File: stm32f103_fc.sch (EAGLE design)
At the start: 39 parts, among them IC1 STM32F10XCXT6, U1 RT9193-33GB, Y1 8MHz, Y2 32.768MHz

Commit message: added more lable
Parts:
- removed C5, C6, C7, C8: 1nF, SparkFun-Capacitors:1.0NF/1000PF-0603-50V-10%
- added C22: 100nF, SparkFun-Capacitors:1.0NF/1000PF-0603-50V-10%
- added SWD: (no value), SparkFun-Connectors:CONN_04
- C1: value 1nF -> 100nF
- C12: value 0.1uF -> 1000nF
- C2: value 1nF -> 10uF
- R3, R4: value 1k -> 70ohm
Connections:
- new net N$28: IC1POWER.VSS_2
- new net N$30: IC1POWER.VDD_2
- new net N$31: IC1POWER.VDD_1
- new net PA0: IC1PORTA_L.PA0
- new net PA1: IC1PORTA_L.PA1
- new net PA10: IC1PORTA_H.PA10
- new net PA15: IC1PORTA_H.PA15
- new net PA2: IC1PORTA_L.PA2
- new net PA3: IC1PORTA_L.PA3
- new net PA4: IC1PORTA_L.PA4
- new net PA5: IC1PORTA_L.PA5
- new net PA6: IC1PORTA_L.PA6
- new net PA7: IC1PORTA_L.PA7
- new net PA8: IC1PORTA_H.PA8
- new net PA9: IC1PORTA_H.PA9
- new net PB0: IC1PORTB_L.PB0
- new net PB1: IC1PORTB_L.PB1
- new net PB10: IC1PORTB_H.PB10
- new net PB11: IC1PORTB_H.PB11
- new net PB12: IC1PORTB_H.PB12
- new net PB13: IC1PORTB_H.PB13
- new net PB14: IC1PORTB_H.PB14
- new net PB15: IC1PORTB_H.PB15
- new net PB3: IC1PORTB_L.PB3
- new net PB4: IC1PORTB_L.PB4
- new net PB5: IC1PORTB_L.PB5
- new net PB6: IC1PORTB_L.PB6
- new net PB7: IC1PORTB_L.PB7
- new net PB8: IC1PORTB_H.PB8
- new net PB9: IC1PORTB_H.PB9
- new net SWDCLK: IC1PORTA_H.PA14, SWD.2
- new net SWDIO: IC1PORTA_H.PA13, SWD.3
- new net VBAT: IC1AN_POWER.VBAT
- net GND: now also C22.2, IC1AN_POWER.VSSA, IC1POWER.VSS_1, IC1POWER.VSS_3, SWD.1
- net PC14: now also IC1PORTC.PC14
- net PC15: now also IC1PORTC.PC15
- net VCC3V3: now also C22.1, IC1AN_POWER.VDDA, SWD.4
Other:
- moved on the sheet: C9, J1

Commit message: added more lable
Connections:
- net 5V: now also J2.3
- net GND: now also J1.1, J1.2, J2.2
- net PA0: now also J1.16
- net PA1: now also J1.15
- net PA10: now also J2.14
- net PA11: now also J2.13
- net PA12: now also J2.12
- net PA15: now also J2.11
- net PA2: now also J1.14
- net PA3: now also J1.13
- net PA4: now also J1.12
- net PA5: now also J1.11
- net PA6: now also J1.10
- net PA7: now also J1.9
- net PA8: now also J2.16
- net PA9: now also J2.15
- net PB0: now also J1.8
- net PB1: now also J1.7
- net PB10: now also J1.6
- net PB11: now also J1.5
- net PB12: now also J2.20
- net PB13: now also J2.19
- net PB14: now also J2.18
- net PB15: now also J2.17
- net PB3: now also J2.10
- net PB4: now also J2.9
- net PB5: now also J2.8
- net PB6: now also J2.7
- net PB7: now also J2.6
- net PB8: now also J2.5
- net PB9: now also J2.4
- net PC13: now also J1.19
- net PC14: now also J1.18
- net PC15: now also J1.17
- net RESET: now also J1.4
- net VBAT: now also J1.20
- net VCC3V3: now also J1.3, J2.1
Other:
- moved on the sheet: J1, J2

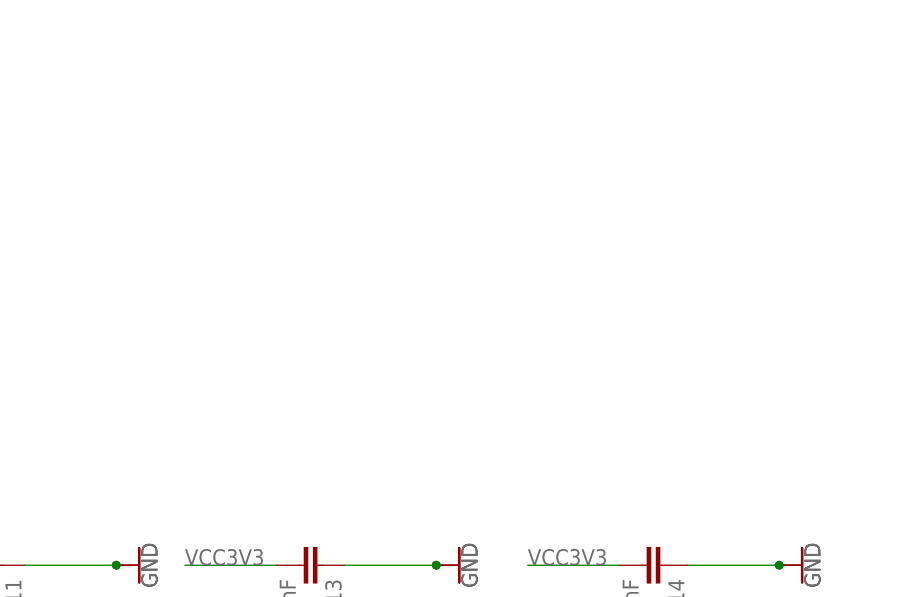
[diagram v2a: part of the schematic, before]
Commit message: added mpu-9250
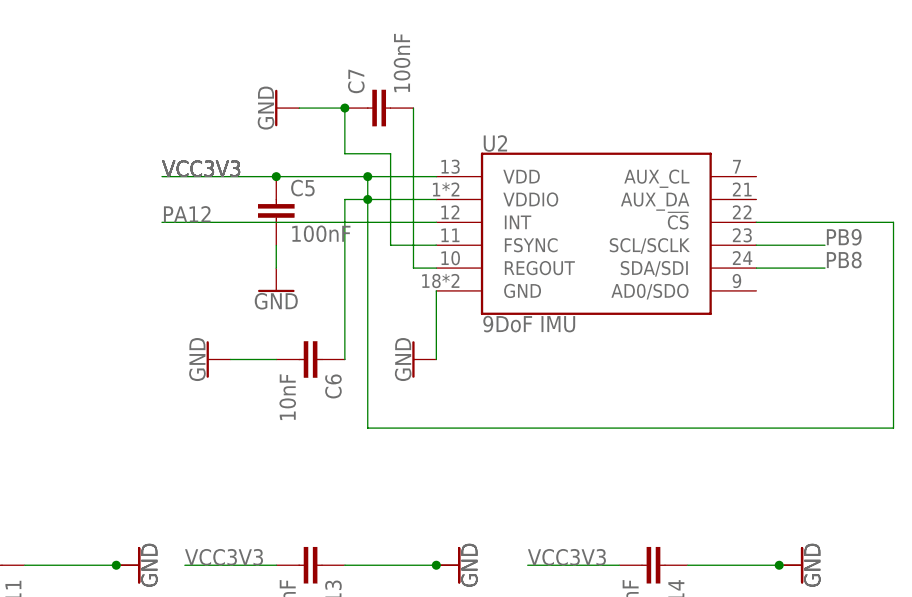
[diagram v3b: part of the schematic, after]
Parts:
- added C5, C7: 100nF, SparkFun-Capacitors:1.0UF-0805-25V-(+80/-20%)
- added C6: 10nF, SparkFun-Capacitors:1.0UF-0805-25V-(+80/-20%)
- added U2: 9DoF IMU, SparkFun-Sensors:MPU-9250
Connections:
- new net N$11: C7.2, U2.REGOUT
- net GND: now also C5.2, C6.2, C7.1, U2.FSYNC, U2.GND
- net PA12: now also U2.INT
- net PB8: now also U2.SDA/SDI
- net PB9: now also U2.SCL/SCLK
- net VCC3V3: now also C5.1, C6.1, U2.!CS, U2.VDD, U2.VDDIO
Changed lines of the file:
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@@
 <part name="GND23" library="SparkFun-PowerSymbols" library_urn="urn:adsk.eagle:library:530" deviceset="GND" device=""/>
 <part name="GND24" library="SparkFun-PowerSymbols" library_urn="urn:adsk.eagle:library:530" deviceset="GND" device=""/>
+<part name="U2" library="SparkFun-Sensors" deviceset="MPU-9250" device="" value="9DoF IMU"/>
+<part name="C5" library="SparkFun-Capacitors" library_urn="urn:adsk.eagle:library:510" deviceset="1.0UF" device="-0805-25V-(+80/-20%)" package3d_urn="urn:adsk.eagle:package:37429/1" value="100nF"/>
+<part name="GND25" library="SparkFun-PowerSymbols" library_urn="urn:adsk.eagle:library:530" deviceset="GND" device=""/>
+<part name="GND26" library="SparkFun-PowerSymbols" library_urn="urn:adsk.eagle:library:530" deviceset="GND" device=""/>
+<part name="C6" library="SparkFun-Capacitors" library_urn="urn:adsk.eagle:library:510" deviceset="1.0UF" device="-0805-25V-(+80/-20%)" package3d_urn="urn:adsk.eagle:package:37429/1" value="10nF"/>
+<part name="GND27" library="SparkFun-PowerSymbols" library_urn="urn:adsk.eagle:library:530" deviceset="GND" device=""/>
+<part name="C7" library="SparkFun-Capacitors" library_urn="urn:adsk.eagle:library:510" deviceset="1.0UF" device="-0805-25V-(+80/-20%)" package3d_urn="urn:adsk.eagle:package:37429/1" value="100nF"/>
+<part name="GND28" library="SparkFun-PowerSymbols" library_urn="urn:adsk.eagle:library:530" deviceset="GND" device=""/>
 </parts>
 <sheets>
@@
 <instance part="GND24" gate="1" x="22.86" y="7.62" smashed="yes" rot="R270">
 <attribute name="VALUE" x="22.606" y="7.62" size="1.778" layer="96" rot="R270" align="top-center"/>
+</instance>
+<instance part="U2" gate="G$1" x="175.26" y="127" smashed="yes">
+<attribute name="NAME" x="162.56" y="137.414" size="1.778" layer="95" font="vector"/>
+<attribute name="VALUE" x="162.56" y="119.126" size="1.778" layer="96" font="vector" align="top-left"/>
+</instance>
+<instance part="C5" gate="G$1" x="139.7" y="129.54" smashed="yes">
+<attribute name="NAME" x="141.224" y="132.461" size="1.778" layer="95" font="vector"/>
+<attribute name="VALUE" x="141.224" y="127.381" size="1.778" layer="96" font="vector"/>
+</instance>
+<instance part="GND25" gate="1" x="139.7" y="121.92" smashed="yes">
+<attribute name="VALUE" x="139.7" y="121.666" size="1.778" layer="96" align="top-center"/>
+</instance>
+<instance part="GND26" gate="1" x="154.94" y="114.3" smashed="yes" rot="R270">
+<attribute name="VALUE" x="154.686" y="114.3" size="1.778" layer="96" rot="R270" align="top-center"/>
+</instance>
+<instance part="C6" gate="G$1" x="142.24" y="114.3" smashed="yes" rot="R270">
+<attribute name="NAME" x="145.161" y="112.776" size="1.778" layer="95" font="vector" rot="R270"/>
+<attribute name="VALUE" x="140.081" y="112.776" size="1.778" layer="96" font="vector" rot="R270"/>
+</instance>
+<instance part="GND27" gate="1" x="132.08" y="114.3" smashed="yes" rot="R270">
+<attribute name="VALUE" x="131.826" y="114.3" size="1.778" layer="96" rot="R270" align="top-center"/>
+</instance>
+<instance part="C7" gate="G$1" x="152.4" y="142.24" smashed="yes" rot="R90">
+<attribute name="NAME" x="149.479" y="143.764" size="1.778" layer="95" font="vector" rot="R90"/>
+<attribute name="VALUE" x="154.559" y="143.764" size="1.778" layer="96" font="vector" rot="R90"/>
+</instance>
+<instance part="GND28" gate="1" x="139.7" y="142.24" smashed="yes" rot="R270">
+<attribute name="VALUE" x="139.446" y="142.24" size="1.778" layer="96" rot="R270" align="top-center"/>
 </instance>
 </instances>
@@
 <wire x1="-63.5" y1="58.42" x2="-71.12" y2="58.42" width="0.1524" layer="91"/>
 <label x="-71.12" y="58.42" size="1.778" layer="95"/>
+</segment>
+<segment>
+<pinref part="U2" gate="G$1" pin="VDD"/>
+<wire x1="157.48" y1="134.62" x2="149.86" y2="134.62" width="0.1524" layer="91"/>
+<label x="127" y="134.62" size="1.778" layer="95"/>
+<label x="127" y="134.62" size="1.778" layer="95"/>
+<label x="127" y="134.62" size="1.778" layer="95"/>
+<label x="127" y="134.62" size="1.778" layer="95"/>
+<pinref part="C5" gate="G$1" pin="1"/>
+<wire x1="149.86" y1="134.62" x2="139.7" y2="134.62" width="0.1524" layer="91"/>
+<wire x1="139.7" y1="134.62" x2="127" y2="134.62" width="0.1524" layer="91"/>
+<junction x="139.7" y="134.62"/>
+<pinref part="U2" gate="G$1" pin="!CS"/>
+<wire x1="193.04" y1="129.54" x2="208.28" y2="129.54" width="0.1524" layer="91"/>
+<wire x1="208.28" y1="129.54" x2="208.28" y2="106.68" width="0.1524" layer="91"/>
+<wire x1="208.28" y1="106.68" x2="149.86" y2="106.68" width="0.1524" layer="91"/>
+<wire x1="149.86" y1="106.68" x2="149.86" y2="132.08" width="0.1524" layer="91"/>
+<pinref part="U2" gate="G$1" pin="VDDIO"/>
+<wire x1="149.86" y1="132.08" x2="157.48" y2="132.08" width="0.1524" layer="91"/>
+<wire x1="149.86" y1="132.08" x2="147.32" y2="132.08" width="0.1524" layer="91"/>
+<junction x="149.86" y="132.08"/>
+<wire x1="149.86" y1="132.08" x2="149.86" y2="134.62" width="0.1524" layer="91"/>
+<junction x="149.86" y="134.62"/>
+<wire x1="147.32" y1="132.08" x2="147.32" y2="114.3" width="0.1524" layer="91"/>
+<pinref part="C6" gate="G$1" pin="1"/>
 </segment>
 </net>
@@
 <pinref part="J2" gate="G$1" pin="2"/>
 </segment>
+<segment>
+<pinref part="C5" gate="G$1" pin="2"/>
+<pinref part="GND25" gate="1" pin="GND"/>
+<wire x1="139.7" y1="127" x2="139.7" y2="124.46" width="0.1524" layer="91"/>
+</segment>
+<segment>
+<pinref part="U2" gate="G$1" pin="GND"/>
+<wire x1="157.48" y1="121.92" x2="157.48" y2="114.3" width="0.1524" layer="91"/>
+<pinref part="GND26" gate="1" pin="GND"/>
+</segment>
+<segment>
+<pinref part="C6" gate="G$1" pin="2"/>
+<pinref part="GND27" gate="1" pin="GND"/>
+<wire x1="139.7" y1="114.3" x2="134.62" y2="114.3" width="0.1524" layer="91"/>
+</segment>
+<segment>
+<pinref part="C7" gate="G$1" pin="1"/>
+<pinref part="GND28" gate="1" pin="GND"/>
+<wire x1="142.24" y1="142.24" x2="147.32" y2="142.24" width="0.1524" layer="91"/>
+<pinref part="U2" gate="G$1" pin="FSYNC"/>
+<wire x1="157.48" y1="127" x2="152.4" y2="127" width="0.1524" layer="91"/>
+<wire x1="152.4" y1="127" x2="152.4" y2="137.16" width="0.1524" layer="91"/>
+<wire x1="152.4" y1="137.16" x2="147.32" y2="137.16" width="0.1524" layer="91"/>
+<wire x1="147.32" y1="137.16" x2="147.32" y2="142.24" width="0.1524" layer="91"/>
+<junction x="147.32" y="142.24"/>
+</segment>
 </net>
 <net name="5V" class="0">
@@
 <pinref part="J2" gate="G$1" pin="12"/>
 </segment>
+<segment>
+<pinref part="U2" gate="G$1" pin="INT"/>
+<wire x1="157.48" y1="129.54" x2="127" y2="129.54" width="0.1524" layer="91"/>
+<label x="127" y="129.54" size="1.778" layer="95"/>
+</segment>
 </net>
 <net name="N$7" class="0">
@@
 <pinref part="J2" gate="G$1" pin="5"/>
 </segment>
+<segment>
+<pinref part="U2" gate="G$1" pin="SDA/SDI"/>
+<wire x1="193.04" y1="124.46" x2="200.66" y2="124.46" width="0.1524" layer="91"/>
+<label x="200.66" y="124.46" size="1.778" layer="95"/>
+</segment>
 </net>
 <net name="PB9" class="0">
@@
 <pinref part="J2" gate="G$1" pin="4"/>
 </segment>
+<segment>
+<pinref part="U2" gate="G$1" pin="SCL/SCLK"/>
+<wire x1="193.04" y1="127" x2="200.66" y2="127" width="0.1524" layer="91"/>
+<label x="200.66" y="127" size="1.778" layer="95"/>
+</segment>
 </net>
 <net name="PB10" class="0">
@@
 </segment>
 </net>
+<net name="N$11" class="0">
+<segment>
+<pinref part="U2" gate="G$1" pin="REGOUT"/>
+<wire x1="157.48" y1="124.46" x2="154.94" y2="124.46" width="0.1524" layer="91"/>
+<pinref part="C7" gate="G$1" pin="2"/>
+<wire x1="154.94" y1="124.46" x2="154.94" y2="142.24" width="0.1524" layer="91"/>
+</segment>
+</net>

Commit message: done some auto routing
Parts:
- added J4: (no value), SparkFun-Connectors:CONN_023.5MM
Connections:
- net 5V: now also J4.2
- net GND: now also J4.1
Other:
- note added: "to IMU clk"
- note added: "to IMU data"
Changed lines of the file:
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@@
 <part name="GND6" library="SparkFun-PowerSymbols" library_urn="urn:adsk.eagle:library:530" deviceset="GND" device=""/>
 <part name="GND7" library="SparkFun-PowerSymbols" library_urn="urn:adsk.eagle:library:530" deviceset="GND" device=""/>
-<part name="SUPPLY1" library="SparkFun-PowerSymbols" library_urn="urn:adsk.eagle:library:530" deviceset="5V" device=""/>
 <part name="C3" library="SparkFun-Capacitors" library_urn="urn:adsk.eagle:library:510" deviceset="1.0NF/1000PF" device="-0603-50V-10%" package3d_urn="urn:adsk.eagle:package:37414/1" value="1nF"/>
 <part name="C4" library="SparkFun-Capacitors" library_urn="urn:adsk.eagle:library:510" deviceset="1.0NF/1000PF" device="-0603-50V-10%" package3d_urn="urn:adsk.eagle:package:37414/1" value="1nF"/>
@@
 <part name="C7" library="SparkFun-Capacitors" library_urn="urn:adsk.eagle:library:510" deviceset="1.0UF" device="-0805-25V-(+80/-20%)" package3d_urn="urn:adsk.eagle:package:37429/1" value="100nF"/>
 <part name="GND28" library="SparkFun-PowerSymbols" library_urn="urn:adsk.eagle:library:530" deviceset="GND" device=""/>
+<part name="J4" library="SparkFun-Connectors" library_urn="urn:adsk.eagle:library:513" deviceset="CONN_02" device="3.5MM" package3d_urn="urn:adsk.eagle:package:38050/1"/>
+<part name="GND29" library="SparkFun-PowerSymbols" library_urn="urn:adsk.eagle:library:530" deviceset="GND" device=""/>
 </parts>
 <sheets>
 <sheet>
 <plain>
+<text x="55.88" y="55.88" size="1.778" layer="91">to IMU data</text>
+<text x="55.88" y="53.34" size="1.778" layer="91">to IMU clk</text>
 </plain>
 <instances>
@@
 <attribute name="VALUE" x="50.8" y="101.346" size="1.778" layer="96" align="top-center"/>
 </instance>
-<instance part="SUPPLY1" gate="G$1" x="-25.4" y="132.08" smashed="yes">
-<attribute name="VALUE" x="-25.4" y="134.874" size="1.778" layer="96" align="bottom-center"/>
-</instance>
 <instance part="C3" gate="G$1" x="-25.4" y="119.38" smashed="yes">
 <attribute name="NAME" x="-23.876" y="122.301" size="1.778" layer="95" font="vector"/>
@@
 <instance part="GND28" gate="1" x="139.7" y="142.24" smashed="yes" rot="R270">
 <attribute name="VALUE" x="139.446" y="142.24" size="1.778" layer="96" rot="R270" align="top-center"/>
+</instance>
+<instance part="J4" gate="G$1" x="-66.04" y="137.16" smashed="yes">
+<attribute name="VALUE" x="-68.58" y="132.334" size="1.778" layer="96" font="vector"/>
+<attribute name="NAME" x="-68.58" y="142.748" size="1.778" layer="95" font="vector"/>
+</instance>
+<instance part="GND29" gate="1" x="-45.72" y="129.54" smashed="yes">
+<attribute name="VALUE" x="-45.72" y="129.286" size="1.778" layer="96" align="top-center"/>
 </instance>
 </instances>
@@
 <junction x="147.32" y="142.24"/>
 </segment>
+<segment>
+<pinref part="J4" gate="G$1" pin="1"/>
+<wire x1="-58.42" y1="137.16" x2="-45.72" y2="137.16" width="0.1524" layer="91"/>
+<wire x1="-45.72" y1="137.16" x2="-45.72" y2="132.08" width="0.1524" layer="91"/>
+<pinref part="GND29" gate="1" pin="GND"/>
+</segment>
 </net>
 <net name="5V" class="0">
 <segment>
-<pinref part="SUPPLY1" gate="G$1" pin="5V"/>
+<pinref part="J3" gate="J1" pin="VBUS"/>
+<wire x1="-53.34" y1="93.98" x2="-43.18" y2="93.98" width="0.1524" layer="91"/>
+<label x="-43.18" y="93.98" size="1.778" layer="95"/>
+</segment>
+<segment>
+<pinref part="R8" gate="G$1" pin="1"/>
+<wire x1="-35.56" y1="76.2" x2="-35.56" y2="71.12" width="0.1524" layer="91"/>
+<label x="-35.56" y="71.12" size="1.778" layer="95"/>
+</segment>
+<segment>
+<wire x1="-63.5" y1="53.34" x2="-71.12" y2="53.34" width="0.1524" layer="91"/>
+<label x="-71.12" y="53.34" size="1.778" layer="95"/>
+<pinref part="J2" gate="G$1" pin="3"/>
+</segment>
+<segment>
+<pinref part="J4" gate="G$1" pin="2"/>
+<label x="-45.72" y="139.7" size="1.778" layer="95"/>
 <pinref part="U1" gate="G$1" pin="VIN"/>
 <wire x1="-12.7" y1="127" x2="-17.78" y2="127" width="0.1524" layer="91"/>
 <wire x1="-17.78" y1="127" x2="-25.4" y2="127" width="0.1524" layer="91"/>
-<wire x1="-25.4" y1="127" x2="-25.4" y2="132.08" width="0.1524" layer="91"/>
 <pinref part="C3" gate="G$1" pin="1"/>
 <wire x1="-25.4" y1="127" x2="-25.4" y2="124.46" width="0.1524" layer="91"/>
@@
 <pinref part="C9" gate="G$1" pin="1"/>
 <wire x1="-30.48" y1="127" x2="-35.56" y2="124.46" width="0.1524" layer="91"/>
-</segment>
-<segment>
-<pinref part="J3" gate="J1" pin="VBUS"/>
-<wire x1="-53.34" y1="93.98" x2="-43.18" y2="93.98" width="0.1524" layer="91"/>
-<label x="-43.18" y="93.98" size="1.778" layer="95"/>
-</segment>
-<segment>
-<pinref part="R8" gate="G$1" pin="1"/>
-<wire x1="-35.56" y1="76.2" x2="-35.56" y2="71.12" width="0.1524" layer="91"/>
-<label x="-35.56" y="71.12" size="1.778" layer="95"/>
-</segment>
-<segment>
-<wire x1="-63.5" y1="53.34" x2="-71.12" y2="53.34" width="0.1524" layer="91"/>
-<label x="-71.12" y="53.34" size="1.778" layer="95"/>
-<pinref part="J2" gate="G$1" pin="3"/>
+<wire x1="-58.42" y1="139.7" x2="-25.4" y2="139.7" width="0.1524" layer="91"/>
+<wire x1="-25.4" y1="139.7" x2="-25.4" y2="127" width="0.1524" layer="91"/>
 </segment>
 </net>

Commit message: backup
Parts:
- removed J1, J2: (no value), SparkFun-Connectors:CONN_20
- added J5, J6: 1X2-3.5MM, adafruit:1X2-3.5MM
- added Q1, Q2: (no value), adafruit:MOSFET-NGDS_TO220V
- added R10, R13: 1ohm, SparkFun-Resistors:1KOHM-0603-1/10W-1%
- added R11, R14: 470ohm, SparkFun-Resistors:1KOHM-0603-1/10W-1%
- renumbered J4 to POWER_INPUT, U1 to VOLTAGE_REGULATOR
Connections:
- new net N$12: J5.2, R13.1
- new net N$13: Q2.D, R13.2
- new net N$14: J6.2, R10.1
- new net N$15: Q1.D, R10.2
- net 5V: now also J5.1, J6.1; no longer J2.3
- net GND: now also Q1.S, Q2.S, R11.1, R14.1; no longer J1.1, J1.2, J2.2
- net PA0: no longer J1.16
- net PA1: no longer J1.15
- net PA10: no longer J2.14
- net PA11: no longer J2.13
- net PA12: no longer J2.12
- net PA15: no longer J2.11
- net PA2: no longer J1.14
- net PA3: no longer J1.13
- net PA4: no longer J1.12
- net PA5: no longer J1.11
- net PA6: no longer J1.10
- net PA7: no longer J1.9
- net PA8: no longer J2.16
- net PA9: no longer J2.15
- net PB0: no longer J1.8
- net PB1: no longer J1.7
- net PB10: no longer J1.6
- net PB11: no longer J1.5
- net PB12: no longer J2.20
- net PB13: no longer J2.19
- net PB14: no longer J2.18
- net PB15: no longer J2.17
- net PB3: no longer J2.10
- net PB4: no longer J2.9
- net PB5: no longer J2.8
- net PB6: now also Q2.G, R14.2; no longer J2.7
- net PB7: now also Q1.G, R11.2; no longer J2.6
- net PB8: no longer J2.5
- net PB9: no longer J2.4
- net PC13: no longer J1.19
- net PC14: no longer J1.18
- net PC15: no longer J1.17
- net RESET: no longer J1.4
- net VBAT: no longer J1.20
- net VCC3V3: no longer J1.3, J2.1

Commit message: slim pcb
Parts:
- removed C4: 1nF, SparkFun-Capacitors:1.0NF/1000PF-0603-50V-10%
- removed SW1, SW2: (no value), adafruit:SWITCH_PUSHBUTTONC&K_KSS
- removed VOLTAGE_REGULATOR: RT9193-33GB, RT9193-33GB:RT9193-33GB
- added IC2: LD117AS33TR, v-reg:LD117AS33TR
- added S1: SPST-SMD-5.2, SparkFun-Switches:MOMENTARY-SWITCH-SPST-SMD-5.2-REDUNDANT
- C12: value 1000nF -> 100nF
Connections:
- removed net N$4: C4.1, VOLTAGE_REGULATOR.BP
- net 5V: now also IC2.IN; no longer VOLTAGE_REGULATOR.EN, VOLTAGE_REGULATOR.VIN
- net GND: now also IC2.ADJ, S1.1; no longer C4.2, SW1.P$1, SW2.P$1, VOLTAGE_REGULATOR.GND
- net RESET: now also S1.2; no longer SW1.P$2, SW2.P$2
- net VCC3V3: now also IC2.OUT; no longer VOLTAGE_REGULATOR.VOUT
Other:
- note added: "checked"
- moved on the sheet: C1, C2, POWER_INPUT
